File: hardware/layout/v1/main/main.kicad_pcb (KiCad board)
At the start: 4 copper layers, 49.5 x 76.5 mm, 71 parts, among them J1 KNX bus terminal pins, J2 AUX, J3 DALI, J4 JST-SH 1x10, Q1 MJD45H11, Q2 BC857, Q3 IRLML0060, Q4 BC847, Q5 BC847, Q6 BC847, U1 NCN5130MNTWG, U2 SCT2400TVBR, U3 REM3-2415S/A 24V->15V 3W iso, U4 TLP383(D4BLLTL,E, U5 TLP383(D4BLLTL,E, U6 LM66100, U7 XIAO ESP32C6, Y1 16MHz

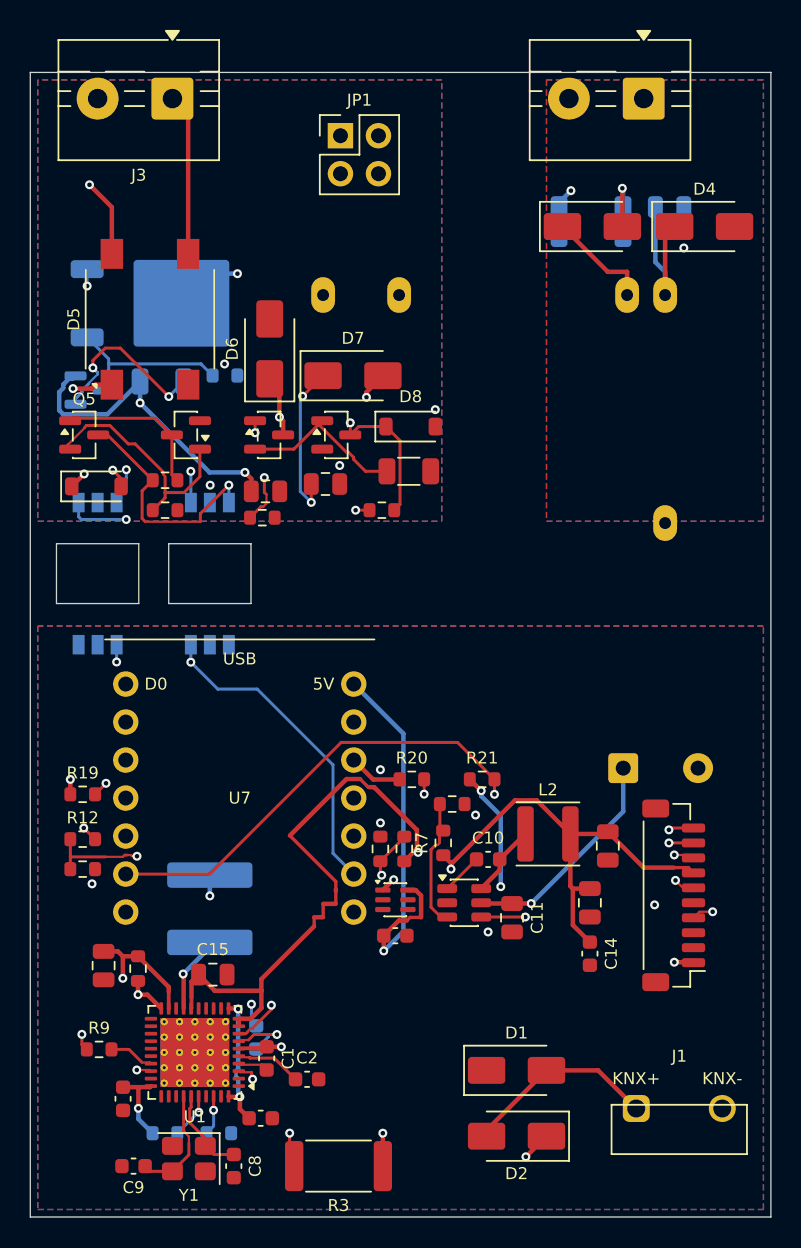
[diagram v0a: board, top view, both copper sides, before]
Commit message: V3 hardware complete: four boards routed and released with 1-DIN enclosure; CI matrix updated; REM3/CTRL supply-off circuit added
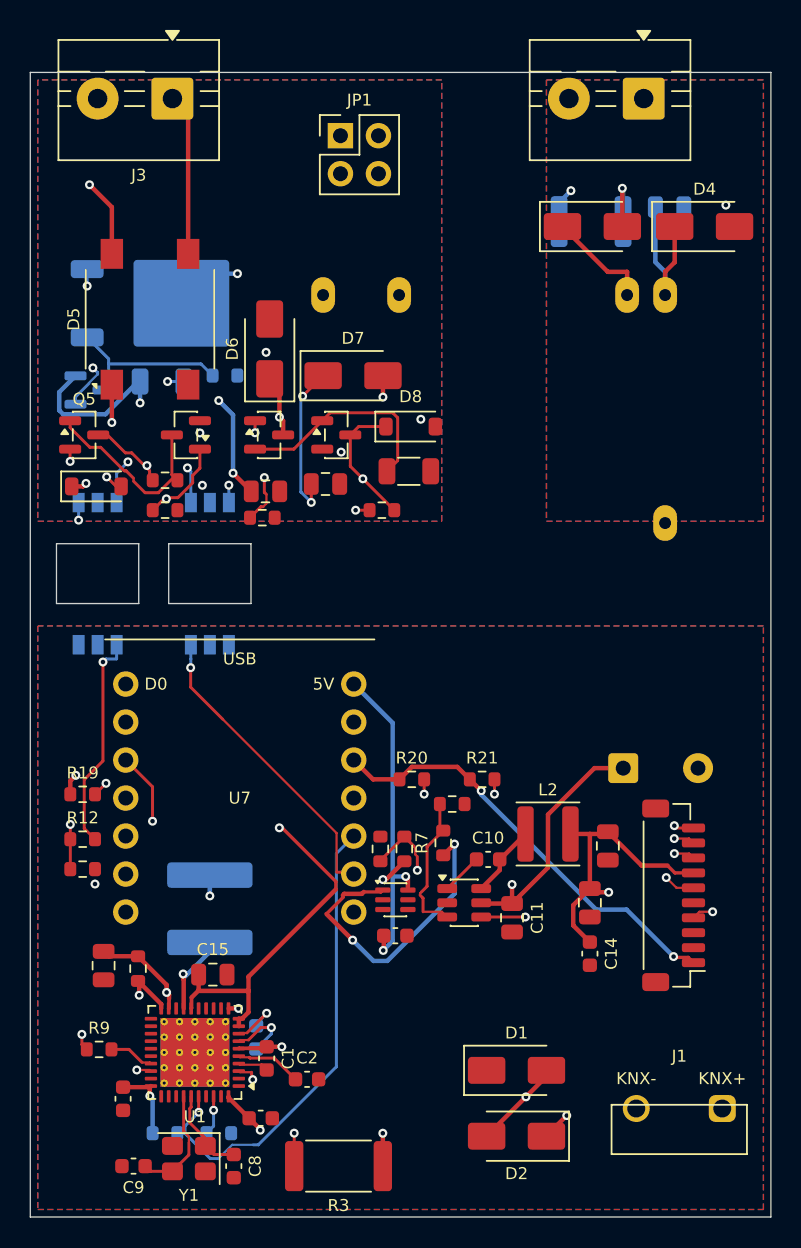
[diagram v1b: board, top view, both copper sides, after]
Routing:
- net I2C_SCL: track 44.6 -> 72.6 mm
- net LED_DATA: track 64.2 -> 45.0 mm
- net +5V: track 37.4 -> 51.2 mm, vias 2 -> 3
- net +3V3: track 63.8 -> 50.0 mm, vias 4 -> 3
- net KNX_P: track 13.1 -> 19.9 mm, vias 0 -> 1
- net I2C_SDA: track 42.2 -> 47.6 mm
- net NCN_SAVEB: track 27.4 -> 32.6 mm
- net +5V_XIAO: track 26.3 -> 22.0 mm, vias 1 -> 2
- net +3V3_TRX: track 39.8 -> 35.6 mm
- net DALI_ISO15V: track 37.2 -> 33.4 mm, vias 2 -> 3
- net DA_P: track 35.3 -> 38.7 mm
- net DALI_SENSE: track 11.2 -> 14.6 mm
- net RX_LIM_IN: track 16.1 -> 12.9 mm, vias 1 -> 2
- net DALI_RX: track 33.5 -> 36.7 mm
- net VFILT: track 63.2 -> 60.4 mm, vias 2 -> 3
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
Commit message: V3 consolidated to two boards (main + ui); updated firmware pin map, button ADC, and OLED connector; removed separate knx/dali boards from CI matrix
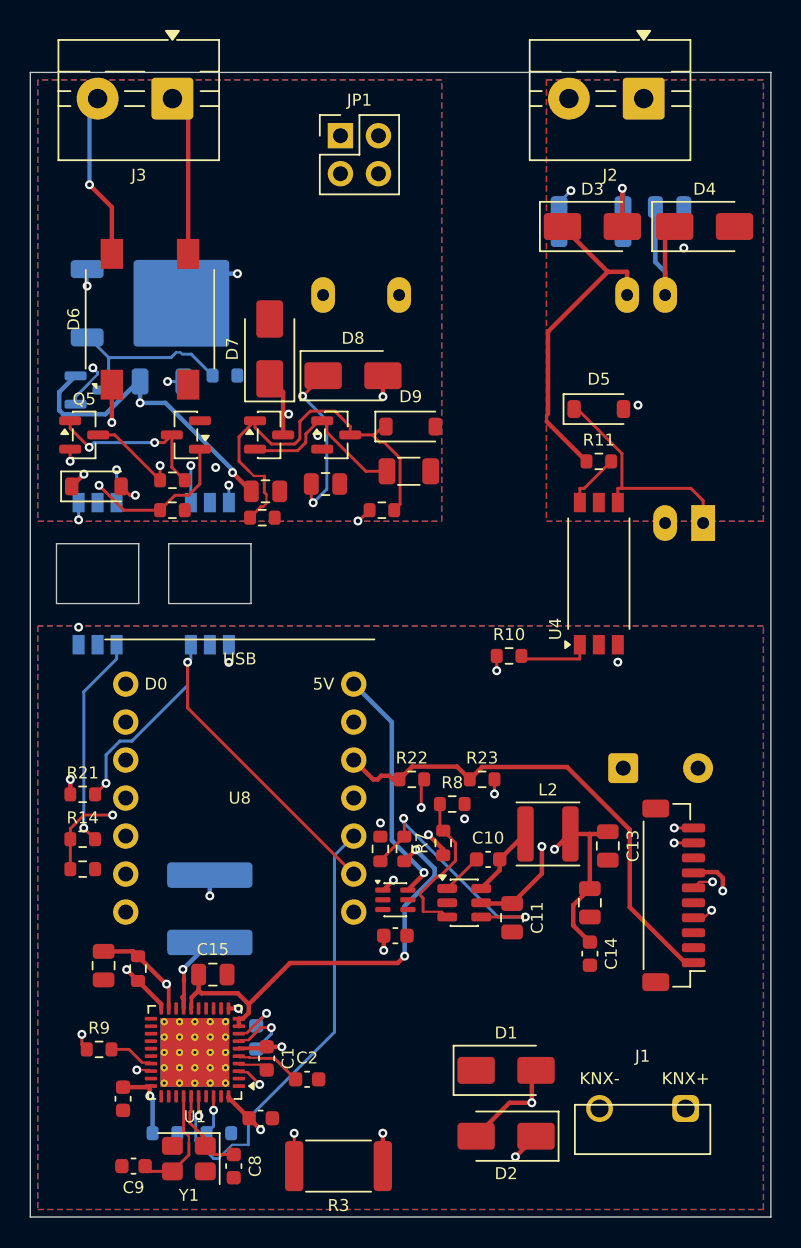
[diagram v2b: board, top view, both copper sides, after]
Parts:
- added D10: 5V6, Diode_SMD:D_SOD-123, F.Cu at (4.42, -48.8)
- added R22: 4k7, Resistor_SMD:R_0603_1608Metric, F.Cu at (25.5, -29.2)
- added R23: 4k7, Resistor_SMD:R_0603_1608Metric, F.Cu at (30.2, -29.2)
- added U8: XIAO ESP32C6, gateway_fp:XIAO_ESP32C6_Header, F.Cu at (14.0, -28.0)
- D5: value DF06S -> 5V6; footprint Diode_SMD:Diode_Bridge_Vishay_DFS -> Diode_SMD:D_SOD-123
- D6: value SMAJ24A -> DF06S; footprint Diode_SMD:D_SMA -> Diode_SMD:Diode_Bridge_Vishay_DFS
- D7: value SS16 -> SMAJ24A
- D8: value 12V -> SS16; footprint Diode_SMD:D_SOD-123 -> Diode_SMD:D_SMA
- D9: value 5V6 -> 12V
- R10: value 3R3 -> 330R; footprint Resistor_SMD:R_1206_3216Metric -> Resistor_SMD:R_0603_1608Metric; moved to F.Cu
- R11: value 4k7 -> 10k; moved to F.Cu
- R12: value 330R -> 3R3; footprint Resistor_SMD:R_0603_1608Metric -> Resistor_SMD:R_1206_3216Metric; moved to B.Cu
- R13: value 10k -> 4k7; moved to B.Cu
- R14: value 22k -> 330R
- R15: value 100k -> 10k
- R16: value 3R3 -> 22k; footprint Resistor_SMD:R_1206_3216Metric -> Resistor_SMD:R_0603_1608Metric
- R18: value 680R -> 3R3; footprint Resistor_SMD:R_0603_1608Metric -> Resistor_SMD:R_1206_3216Metric
- R19: value 10k -> 100k
- R20: value 4k7 -> 680R
- R21: value 4k7 -> 10k
- U3: value REM3-2415S/A 24V->15V 3W iso -> REM3-2415S/A/CTRL 24V->15V 3W iso; footprint gateway_fp:Converter_DCDC_RECOM_REM3_DIP24 -> gateway_fp:Converter_DCDC_RECOM_REM3_DIP24_CTRL
- U4: value TLP383(D4BLLTL,E -> TLP383; moved to F.Cu
- U6: value LM66100 -> TLP383(D4BLLTL,E; footprint Package_TO_SOT_SMD:SOT-363_SC-70-6 -> Package_SO:SO-6L_10x3.84mm_P1.27mm; moved to B.Cu
- U7: value XIAO ESP32C6 -> LM66100; footprint gateway_fp:XIAO_ESP32C6_Header -> Package_TO_SOT_SMD:SOT-363_SC-70-6
- moved R13 34.3 mm to (13.0, -56.2)
- moved U4 33.5 mm to (38.0, -43.0)
- moved R12 31.0 mm to (8.80, -55.8)
- moved D5 30.6 mm to (38.0, -54.0), turned to 0 degrees
- moved R14 29.7 mm to (3.50, -25.2)
- moved R10 29.6 mm to (32.0, -37.5)
- moved R21 26.7 mm to (3.50, -28.2)
- moved R15 26.4 mm to (3.50, -23.2)
- moved R11 25.6 mm to (38.0, -50.5)
- moved U6 25.1 mm to (12.0, -43.0), turned to -90 degrees
- moved R20 24.1 mm to (9.50, -47.2)
- moved R19 21.8 mm to (9.50, -49.2)
- moved D9 21.4 mm to (25.4, -52.8)
- moved R18 16.5 mm to (25.3, -49.8)
- moved U7 12.4 mm to (24.4, -21.2)
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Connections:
- D5 pad 1: DA_P -> N$8
- D5 pad 2: GNDD -> GNDA
- D7 pad 1: DALI_BOOT -> DA_P
- D7 pad 2: DA_P -> GNDD
- D8 pad 1: DALI_GATE -> DALI_BOOT
- D8 pad 2: GNDD -> DA_P
- D9 pad 1: DA_P -> DALI_GATE
- D9 pad 2: N$9 -> GNDD
- J4 pad 8: LED_DALI -> GND
- Q1 pad 1: N$7 -> N$10
- Q1 pad 3: N$6 -> N$9
- Q2 pad 1: N$6 -> N$9
- Q2 pad 3: N$7 -> N$10
- Q5 pad 1: N$11 -> N$14
- Q5 pad 2: N$10 -> N$13
- Q6 pad 1: N$10 -> N$13
- Q6 pad 3: N$11 -> N$14
- R10 pad 1: DALI_ISO15V -> DALI_SUPPLY_OFF
- R11 pad 1: N$7 -> AUX_P
- R11 pad 2: GNDD -> N$7
- R12 pad 1: DALI_TX -> DALI_ISO15V
- R12 pad 2: N$8 -> N$9
- R13 pad 1: DALI_TX -> N$10
- R13 pad 2: GND -> GNDD
- R14 pad 1: DALI_GATE_SW -> DALI_TX
- R14 pad 2: DALI_GATE -> N$11
- R15 pad 1: DALI_GATE -> DALI_TX
- R15 pad 2: GNDD -> GND
- R16 pad 1: DALI_SENSE -> DALI_GATE_SW
- R16 pad 2: GNDD -> DALI_GATE
- R17 pad 1: RX_LIM_IN -> DALI_GATE
- R17 pad 2: N$11 -> GNDD
- R18 pad 1: N$10 -> DALI_SENSE
- R19 pad 1: +3V3 -> RX_LIM_IN
- R19 pad 2: DALI_RX -> N$14
- R20 pad 1: +3V3 -> N$13
- R20 pad 2: I2C_SDA -> GNDD
- R21 pad 2: I2C_SCL -> DALI_RX
- U4 pad 1: N$8 -> N$6
- U4 pad 4: DALI_GATE_SW -> N$8
- U4 pad 6: DALI_BOOT -> N$7
- U5 pad 1: N$9 -> N$11
- U5 pad 3: RX_LIM_IN -> GND
- U5 pad 4: GND -> DALI_GATE_SW
- U5 pad 6: DALI_RX -> DALI_BOOT
- U6 pad 1: +5V -> N$12
- U6 pad 2: GND -> (no net)
- U6 pad 3: GND -> RX_LIM_IN
- U6 pad 4: (no net) -> GND
- U6 pad 6: +5V_XIAO -> DALI_RX
- U7 pad 1: LED_DATA -> +5V
- U7 pad 2: (no net) -> GND
- U7 pad 3: BTN_LADDER -> GND
- U7 pad 4: LED_DALI -> (no net)
- U7 pad 5: I2C_SDA -> (no net)
- U7 pad 6: I2C_SCL -> +5V_XIAO
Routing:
- net LED_DALI: track 43.9 -> 0.00 mm, vias 1 -> 0
- net DALI_SUPPLY_OFF: track 0.00 -> 28.3 mm, vias 0 -> 1
- net I2C_SCL: track 72.6 -> 47.7 mm
- net AUX_P: track 23.8 -> 39.2 mm
- net N$13: track 0.00 -> 14.4 mm, vias 0 -> 2
- net N$14: track 0.00 -> 11.6 mm, vias 0 -> 2
- net N$6: track 16.4 -> 4.94 mm, vias 3 -> 0
- net LED_DATA: track 45.0 -> 53.7 mm
- net N$12: track 0.00 -> 8.20 mm, vias 0 -> 2
- net VFILT: track 60.4 -> 52.2 mm
- net N$7: track 11.5 -> 3.79 mm
- net N$9: track 9.28 -> 16.4 mm, vias 2 -> 3
- net DA_P: track 38.7 -> 32.6 mm
- net DALI_RX: track 36.7 -> 31.9 mm
- net +3V3: track 50.0 -> 54.4 mm, vias 3 -> 1
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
